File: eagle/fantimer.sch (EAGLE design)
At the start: 18 parts, among them IC1 PIC10F220, K1 PB2032-ND, Q1 2N7000-G, U1 IRM-01-5, X1 732-10957-ND

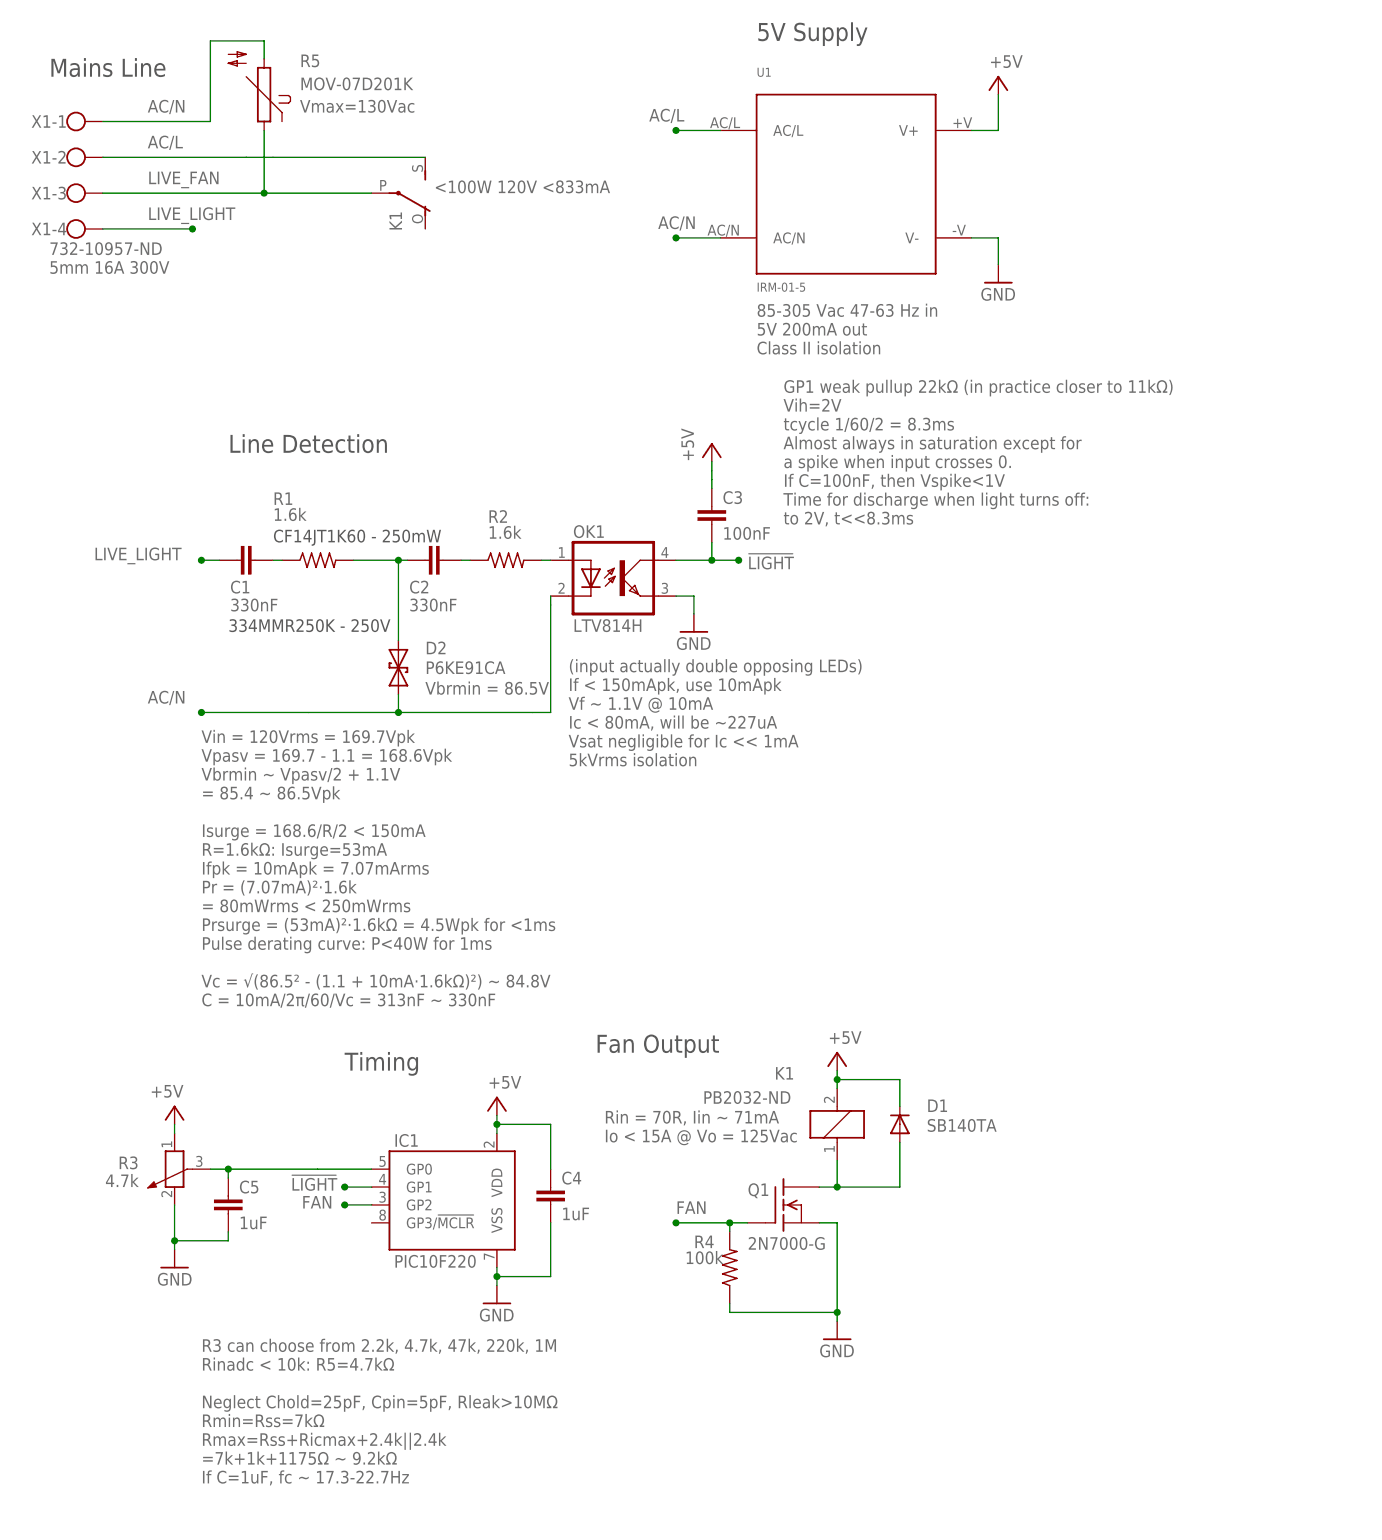
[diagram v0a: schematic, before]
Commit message: - Fix for backward PSU - CPTC fuse added on light line - Filament fuse added on AC/L line - Drop analysis (that goes in the report)
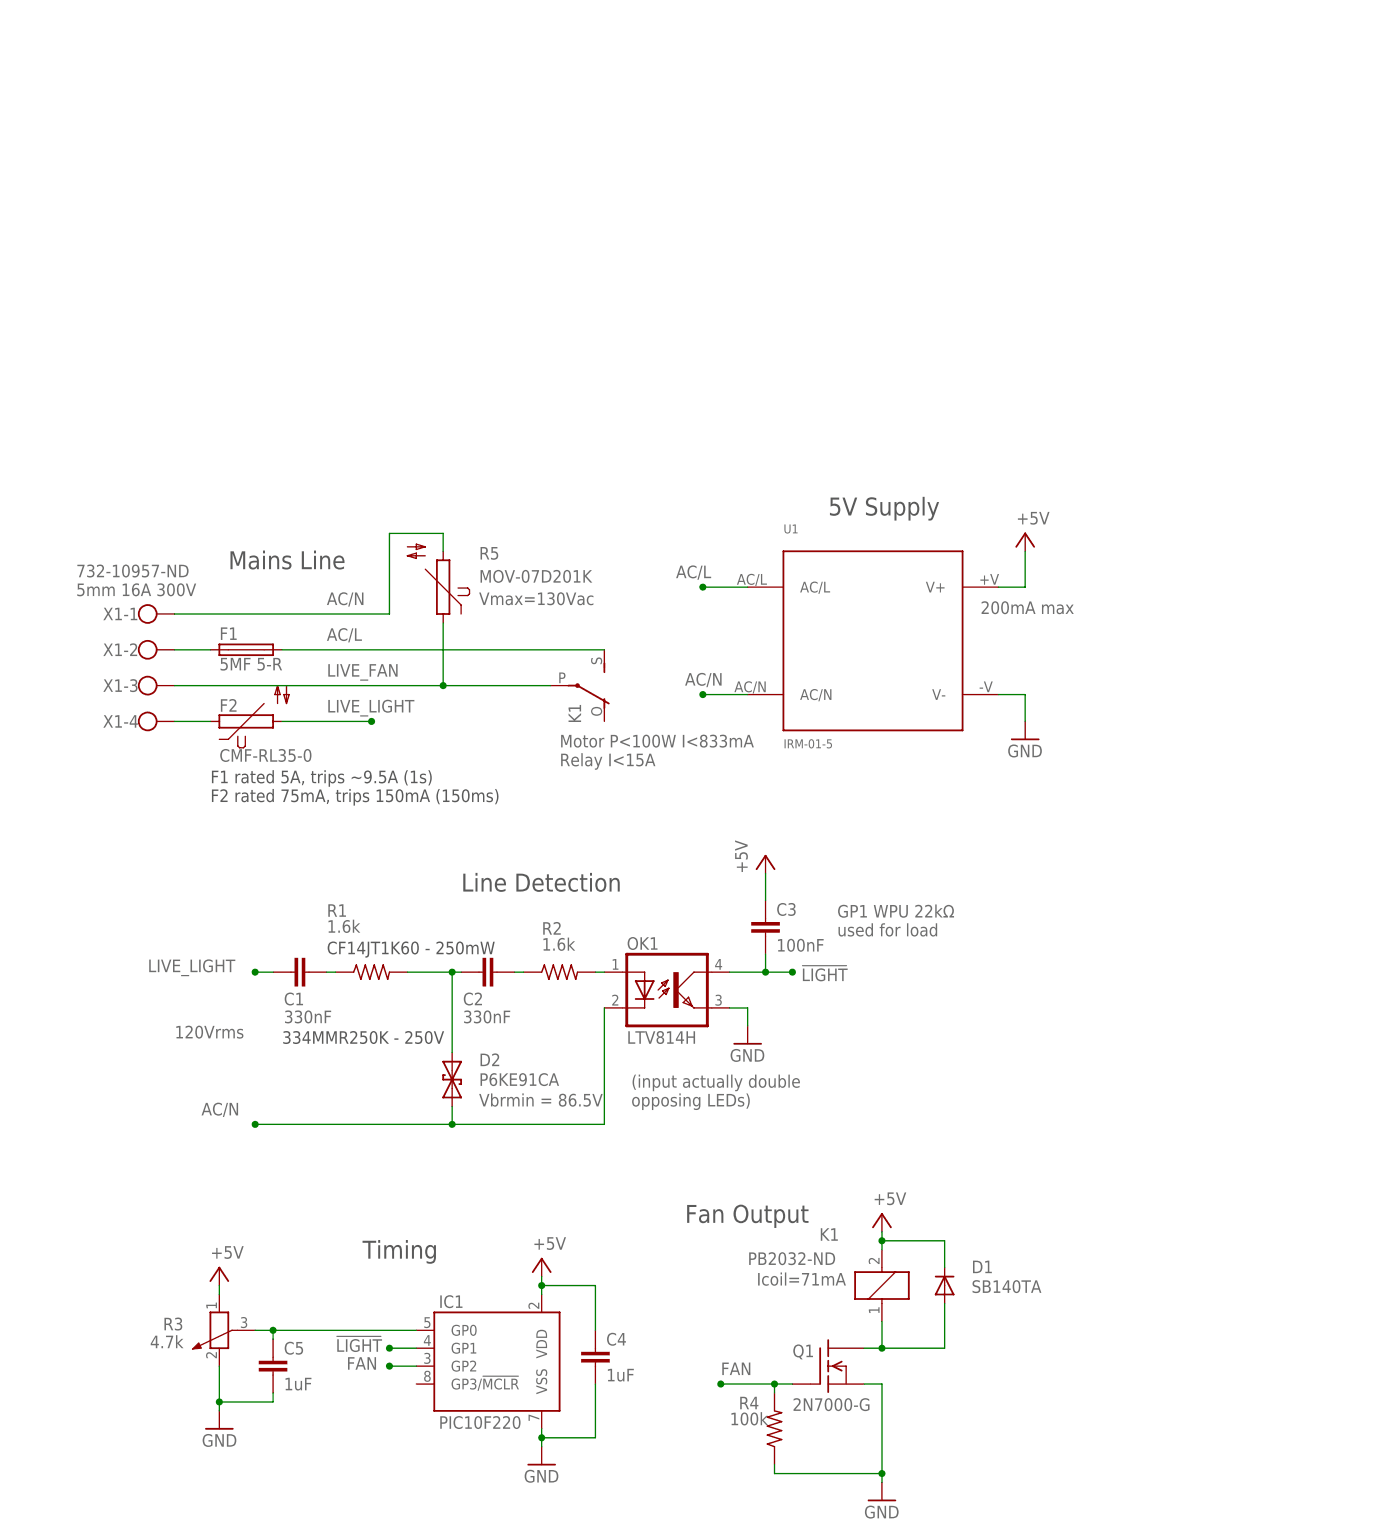
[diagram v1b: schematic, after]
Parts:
- added F1: 5MF 5-R, fuse:FUSESHK20Q
- added F2: CMF-RL35-0, varistor:S05K460
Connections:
- new net AC/L_FUSE: F1.1, X1-2.KL
- new net LIGHT_FUSE: F2.1, X1-4.KL
- net AC/L: now also F1.2; no longer X1-2.KL
- net LIVE_LIGHT: now also F2.2; no longer X1-4.KL
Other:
- note added: "(input actually double opposing LEDs)"
- note added: "120Vrms"
- note added: "200mA max"
- note added: "F1 rated 5A, trips ~9.5A (1s) F2 rated 75mA, trips 150mA (150ms)"
- note added: "GP1 WPU 22kΩ used for load"
- note added: "Icoil=71mA"
- note added: "Motor P<100W I<833mA Relay I<15A"
- note removed: "(input actually double opposing LEDs) If < 150mApk, use 10mApk Vf ~ 1.1V @ 10mA Ic < 80mA, will be ~227uA Vsat negligible for Ic << 1mA 5kVrms isolation"
- note removed: "85-305 Vac 47-63 Hz in 5V 200mA out Class II isolation"
- note removed: "<100W 120V <833mA"
- note removed: "GP1 weak pullup 22kΩ (in practice closer to 11kΩ) Vih=2V tcycle 1/60/2 = 8.3ms Almost always in saturation except for a spike when input crosses 0. If C=100nF, then Vspike<1V Time for discharge when light turns off: to 2V, t<<8.3ms"
- note removed: "R3 can choose from 2.2k, 4.7k, 47k, 220k, 1M Rinadc < 10k: R5=4.7kΩ Neglect Chold=25pF, Cpin=5pF, Rleak>10MΩ Rmin=Rss=7kΩ Rmax=Rss+Ricmax+2.4k||2.4k =7k+1k+1175Ω ~ 9.2kΩ If C=1uF, fc ~ 17.3-22.7Hz"
- note removed: "Rin = 70R, Iin ~ 71mA Io < 15A @ Vo = 125Vac"
- note removed: "Vin = 120Vrms = 169.7Vpk Vpasv = 169.7 - 1.1 = 168.6Vpk Vbrmin ~ Vpasv/2 + 1.1V = 85.4 ~ 86.5Vpk Isurge = 168.6/R/2 < 150mA R=1.6kΩ: Isurge=53mA Ifpk = 10mApk = 7.07mArms Pr = (7.07mA)²·1.6k = 80mWrms < 250mWrms Prsurge = (53mA)²·1.6kΩ = 4.5Wpk for <1ms Pulse derating curve: P<40W for 1ms Vc = √(86.5² - (1.1 + 10mA·1.6kΩ)²) ~ 84.8V C = 10mA/2π/60/Vc = 313nF ~ 330nF"
- moved on the sheet: C1, C2, C3, C4, C5, D1, D2, IC1, K1, OK1, Q1, R1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

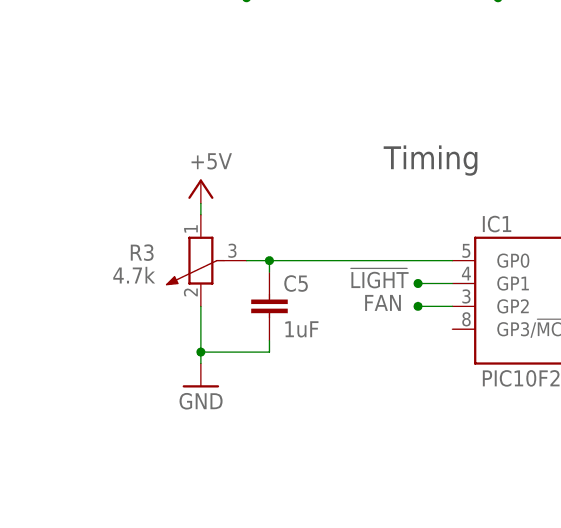
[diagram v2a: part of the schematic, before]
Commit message: Rearrange board taking advantage of ground buses. CPTC is narrower than predicted.
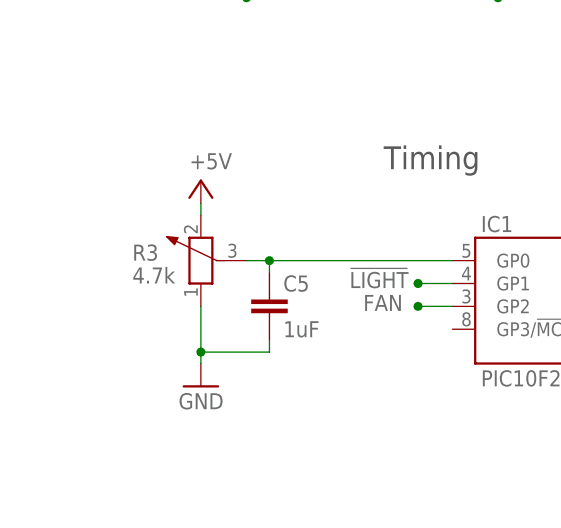
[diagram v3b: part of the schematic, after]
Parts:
- F2: device varistor:S05K460 -> varistor:S05K11
- R5: device varistor:S05K300 -> varistor:S05K11
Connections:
- net +5V: now also R3.2; no longer R3.1
- net GND: now also R3.1; no longer R3.2
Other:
- moved on the sheet: R3
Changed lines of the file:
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@@
 <part name="R4" library="resistor" library_urn="urn:adsk.eagle:library:348" deviceset="R-US_" device="0207/7" package3d_urn="urn:adsk.eagle:package:23493/1" value="100k"/>
 <part name="C4" library="rcl" library_urn="urn:adsk.eagle:library:334" deviceset="C-EU" device="025-025X050" package3d_urn="urn:adsk.eagle:package:23629/2" value="1uF"/>
-<part name="R5" library="varistor" library_urn="urn:adsk.eagle:library:410" deviceset="S05K300" device="" package3d_urn="urn:adsk.eagle:package:30536/1" value="MOV-07D201K"/>
+<part name="R5" library="varistor" library_urn="urn:adsk.eagle:library:410" deviceset="S05K11" device="" package3d_urn="urn:adsk.eagle:package:30524/1" value="MOV-07D201K"/>
 <part name="C5" library="rcl" library_urn="urn:adsk.eagle:library:334" deviceset="C-EU" device="025-025X050" package3d_urn="urn:adsk.eagle:package:23629/2" value="1uF"/>
 <part name="F1" library="fuse" library_urn="urn:adsk.eagle:library:233" deviceset="FUSE" device="SHK20Q" package3d_urn="urn:adsk.eagle:package:14073/1" value="5MF 5-R"/>
-<part name="F2" library="varistor" library_urn="urn:adsk.eagle:library:410" deviceset="S05K460" device="" package3d_urn="urn:adsk.eagle:package:30535/1" value="CMF-RL35-0"/>
+<part name="F2" library="varistor" library_urn="urn:adsk.eagle:library:410" deviceset="S05K11" device="" package3d_urn="urn:adsk.eagle:package:30524/1" value="CMF-RL35-0"/>
 </parts>
 <sheets>
@@
 <attribute name="VALUE" x="25.4" y="79.248" size="1.778" layer="96"/>
 </instance>
-<instance part="R3" gate="1" x="10.16" y="22.86" rot="MR270">
-<attribute name="NAME" x="5.08" y="22.86" size="1.778" layer="95" rot="MR0"/>
-<attribute name="VALUE" x="5.08" y="20.32" size="1.778" layer="96" rot="MR0"/>
+<instance part="R3" gate="1" x="10.16" y="22.86" rot="R90">
+<attribute name="NAME" x="2.54" y="22.86" size="1.778" layer="95"/>
+<attribute name="VALUE" x="2.54" y="20.32" size="1.778" layer="96"/>
 </instance>
 <instance part="P+6" gate="1" x="55.88" y="33.02">
@@
 <pinref part="GND5" gate="1" pin="GND"/>
 <wire x1="10.16" y1="11.43" x2="10.16" y2="12.7" width="0.1524" layer="91"/>
-<pinref part="R3" gate="1" pin="2"/>
 <pinref part="C5" gate="G$1" pin="2"/>
-<wire x1="10.16" y1="12.7" x2="10.16" y2="17.78" width="0.1524" layer="91"/>
 <wire x1="17.78" y1="13.97" x2="17.78" y2="12.7" width="0.1524" layer="91"/>
 <wire x1="17.78" y1="12.7" x2="10.16" y2="12.7" width="0.1524" layer="91"/>
+<pinref part="R3" gate="1" pin="1"/>
+<wire x1="10.16" y1="17.78" x2="10.16" y2="12.7" width="0.1524" layer="91"/>
 <junction x="10.16" y="12.7"/>
 </segment>
@@
 </segment>
 <segment>
-<pinref part="R3" gate="1" pin="1"/>
-<pinref part="P+2" gate="1" pin="+5V"/>
-<wire x1="10.16" y1="27.94" x2="10.16" y2="29.21" width="0.1524" layer="91"/>
-</segment>
-<segment>
 <pinref part="P+6" gate="1" pin="+5V"/>
 <pinref part="IC1" gate="G$1" pin="VDD"/>
@@
 <junction x="55.88" y="29.21"/>
 </segment>
+<segment>
+<pinref part="R3" gate="1" pin="2"/>
+<pinref part="P+2" gate="1" pin="+5V"/>
+<wire x1="10.16" y1="27.94" x2="10.16" y2="29.21" width="0.1524" layer="91"/>
+</segment>
 </net>
 <net name="ADJ" class="0">
 <segment>
-<pinref part="R3" gate="1" pin="3"/>
-<wire x1="15.24" y1="22.86" x2="17.78" y2="22.86" width="0.1524" layer="91"/>
 <pinref part="IC1" gate="G$1" pin="GP0"/>
 <wire x1="17.78" y1="22.86" x2="38.1" y2="22.86" width="0.1524" layer="91"/>
 <pinref part="C5" gate="G$1" pin="1"/>
 <wire x1="17.78" y1="21.59" x2="17.78" y2="22.86" width="0.1524" layer="91"/>
+<pinref part="R3" gate="1" pin="3"/>
+<wire x1="15.24" y1="22.86" x2="17.78" y2="22.86" width="0.1524" layer="91"/>
 <junction x="17.78" y="22.86"/>
 </segment>
